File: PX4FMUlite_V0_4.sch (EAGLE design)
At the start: 126 parts, among them J2 DF13-4P-1.25V, J201 DF13C-6P-1.25V, J202 DF13C-6P-1.25V, J203 DF13C-6P-1.25V, J3 DF13C-4P-1.25V, J302 DF13C-4P-1.25V, J401 DF13C-4P-1.25V, J403 DF13C-7P-1.25V, J405 DF13C-4P-1.25V, J802 DF13C-3P-1.25V, M3_MOUNT1101 MOUNT-HOLE3.1MM, M3_MOUNT1102 MOUNT-HOLE3.1MM, M3_MOUNT1103 MOUNT-HOLE3.1MM, M3_MOUNT1104 MOUNT-HOLE3.1MM, U101 STM32F4X7VX, U2 MAX3051, U401 MAX3051, X101 3.2x2.5 mm / 24 MHz / 15 ppm

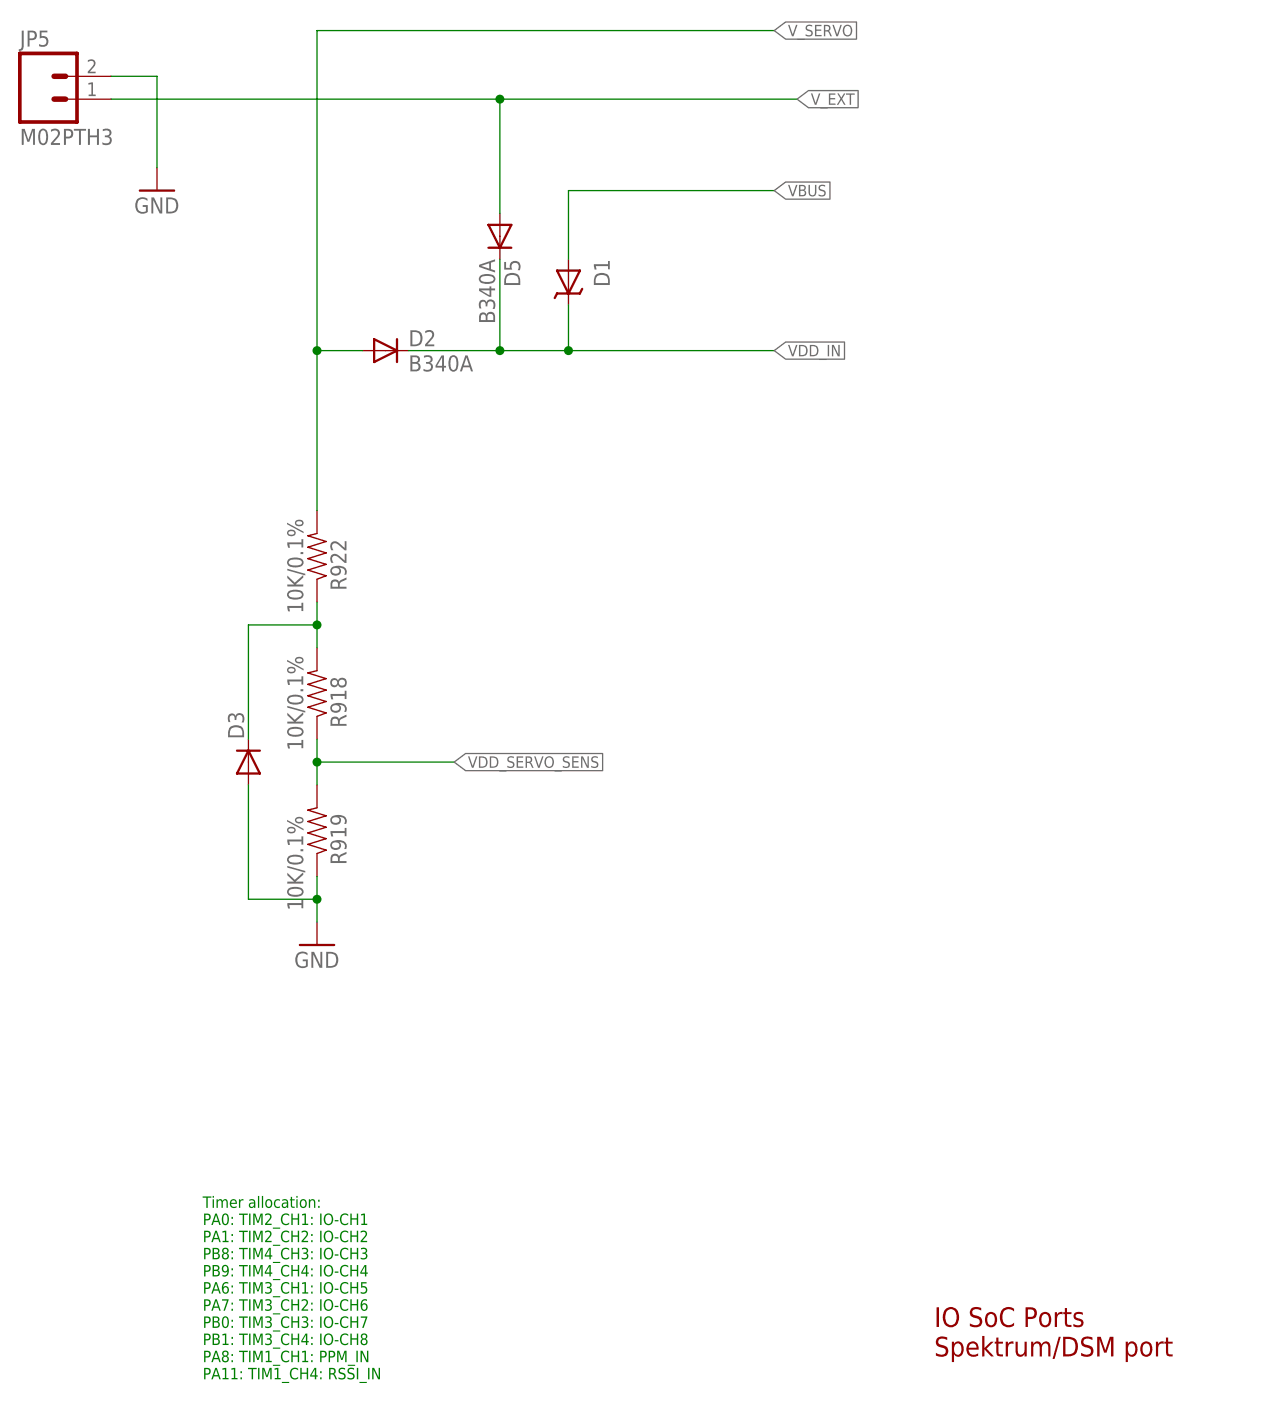
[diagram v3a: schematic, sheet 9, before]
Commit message: Voltage sense moved from VSERVO to VAUX
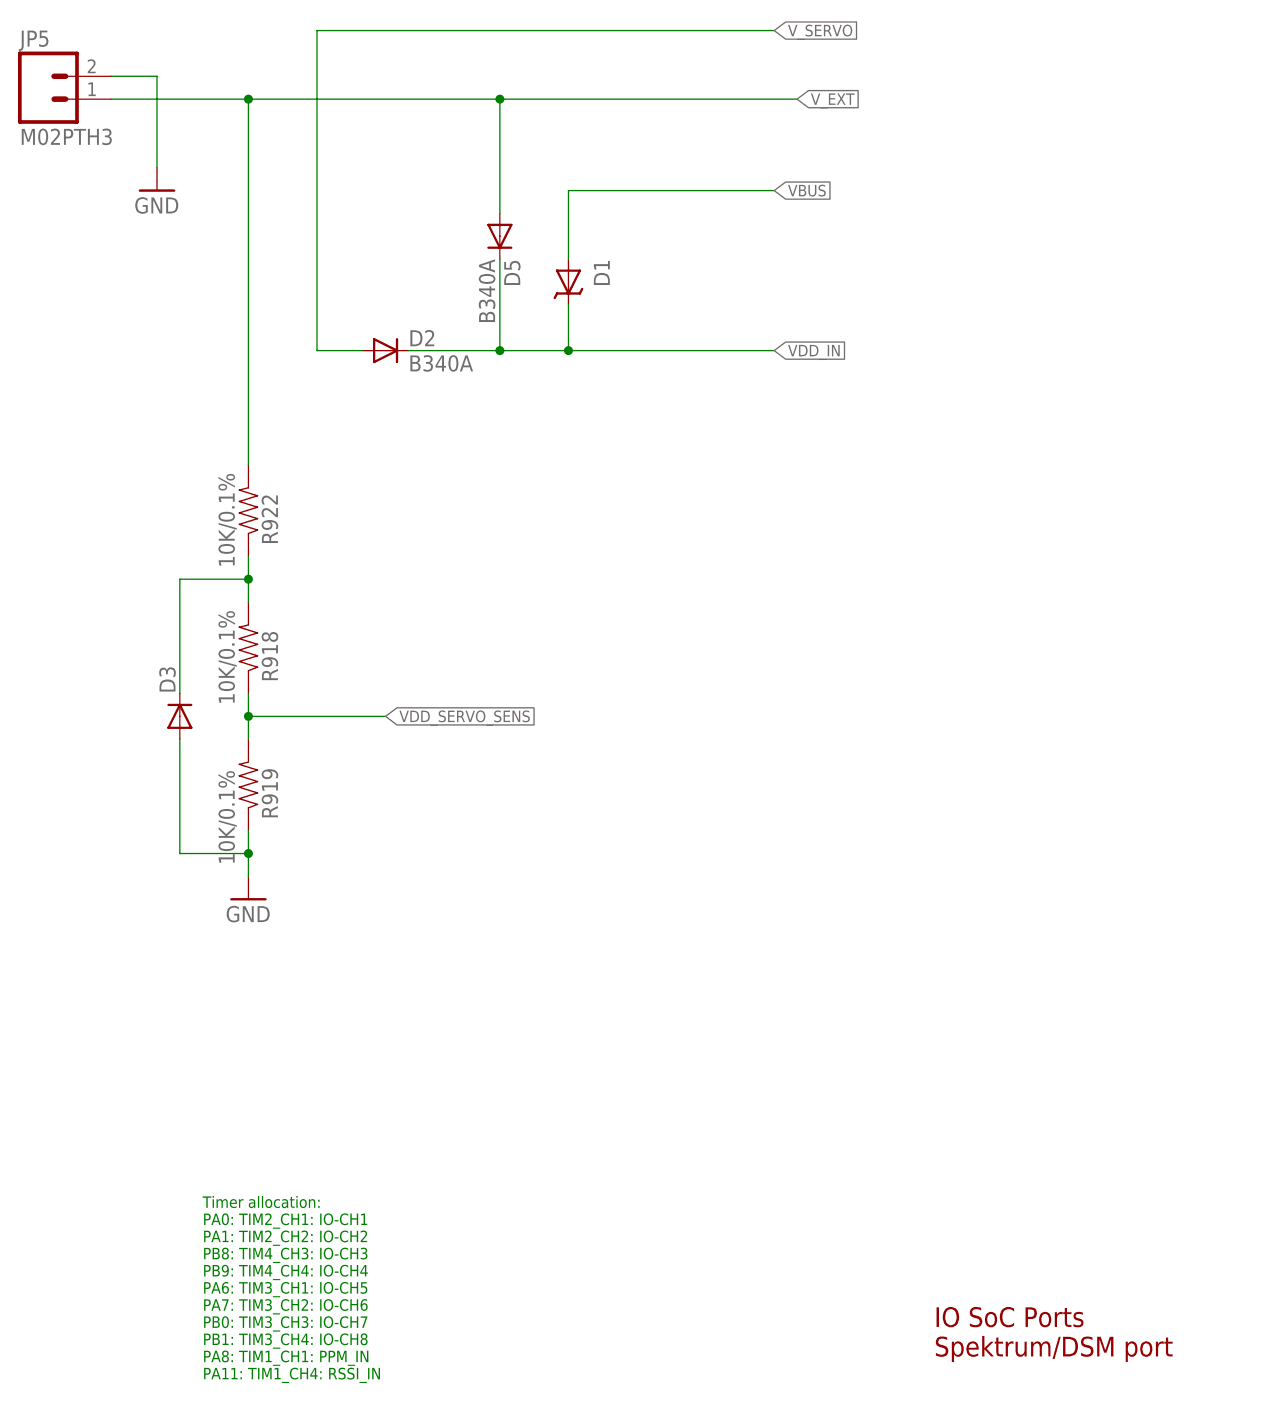
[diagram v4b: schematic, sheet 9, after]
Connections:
- net V_EXT: now also R922.2
- net V_SERVO: no longer R922.2
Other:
- moved on the sheet: D3, R918, R919, R922
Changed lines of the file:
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@@
 <instances>
 <instance part="FRAME4" gate="G$1" x="0" y="0"/>
-<instance part="R918" gate="G$1" x="96.52" y="88.9" smashed="yes" rot="MR90">
-<attribute name="PARTNO" x="96.52" y="88.9" size="1.778" layer="96" rot="MR90" display="off"/>
-<attribute name="NAME" x="98.0186" y="85.09" size="1.778" layer="95" rot="MR90"/>
-<attribute name="VALUE" x="93.218" y="82.55" size="1.778" layer="96" rot="MR90"/>
+<instance part="R918" gate="G$1" x="88.9" y="93.98" smashed="yes" rot="MR90">
+<attribute name="PARTNO" x="88.9" y="93.98" size="1.778" layer="96" rot="MR90" display="off"/>
+<attribute name="NAME" x="90.3986" y="90.17" size="1.778" layer="95" rot="MR90"/>
+<attribute name="VALUE" x="85.598" y="87.63" size="1.778" layer="96" rot="MR90"/>
 </instance>
-<instance part="R919" gate="G$1" x="96.52" y="73.66" smashed="yes" rot="MR90">
-<attribute name="PARTNO" x="96.52" y="73.66" size="1.778" layer="96" rot="MR90" display="off"/>
-<attribute name="NAME" x="98.0186" y="69.85" size="1.778" layer="95" rot="MR90"/>
-<attribute name="VALUE" x="93.218" y="64.77" size="1.778" layer="96" rot="MR90"/>
+<instance part="R919" gate="G$1" x="88.9" y="78.74" smashed="yes" rot="MR90">
+<attribute name="PARTNO" x="88.9" y="78.74" size="1.778" layer="96" rot="MR90" display="off"/>
+<attribute name="NAME" x="90.3986" y="74.93" size="1.778" layer="95" rot="MR90"/>
+<attribute name="VALUE" x="85.598" y="69.85" size="1.778" layer="96" rot="MR90"/>
 </instance>
-<instance part="GND52" gate="1" x="96.52" y="60.96"/>
-<instance part="R922" gate="G$1" x="96.52" y="104.14" smashed="yes" rot="MR90">
-<attribute name="PARTNO" x="96.52" y="104.14" size="1.778" layer="96" rot="MR90" display="off"/>
-<attribute name="NAME" x="98.0186" y="100.33" size="1.778" layer="95" rot="MR90"/>
-<attribute name="VALUE" x="93.218" y="97.79" size="1.778" layer="96" rot="MR90"/>
+<instance part="GND52" gate="1" x="88.9" y="66.04"/>
+<instance part="R922" gate="G$1" x="88.9" y="109.22" smashed="yes" rot="MR90">
+<attribute name="PARTNO" x="88.9" y="109.22" size="1.778" layer="96" rot="MR90" display="off"/>
+<attribute name="NAME" x="90.3986" y="105.41" size="1.778" layer="95" rot="MR90"/>
+<attribute name="VALUE" x="85.598" y="102.87" size="1.778" layer="96" rot="MR90"/>
 </instance>
 <instance part="D1" gate="G$1" x="124.46" y="134.62" smashed="yes" rot="MR270">
@@
 <attribute name="PARTNO" x="124.46" y="134.62" size="1.778" layer="96" rot="MR90" display="off"/>
 </instance>
-<instance part="D3" gate="G$1" x="88.9" y="81.28" rot="R90"/>
+<instance part="D3" gate="G$1" x="81.28" y="86.36" rot="R90"/>
 <instance part="D2" gate="G$1" x="104.14" y="127"/>
 <instance part="D5" gate="G$1" x="116.84" y="139.7" rot="R270"/>
@@
 <pinref part="GND52" gate="1" pin="GND"/>
 <pinref part="R919" gate="G$1" pin="1"/>
-<wire x1="96.52" y1="63.5" x2="96.52" y2="66.04" width="0.1524" layer="91"/>
+<wire x1="88.9" y1="68.58" x2="88.9" y2="71.12" width="0.1524" layer="91"/>
 <pinref part="D3" gate="G$1" pin="A"/>
-<wire x1="96.52" y1="66.04" x2="96.52" y2="68.58" width="0.1524" layer="91"/>
-<wire x1="96.52" y1="66.04" x2="88.9" y2="66.04" width="0.1524" layer="91"/>
-<wire x1="88.9" y1="66.04" x2="88.9" y2="78.74" width="0.1524" layer="91"/>
-<junction x="96.52" y="66.04"/>
+<wire x1="88.9" y1="71.12" x2="88.9" y2="73.66" width="0.1524" layer="91"/>
+<wire x1="88.9" y1="71.12" x2="81.28" y2="71.12" width="0.1524" layer="91"/>
+<wire x1="81.28" y1="71.12" x2="81.28" y2="83.82" width="0.1524" layer="91"/>
+<junction x="88.9" y="71.12"/>
 </segment>
 <segment>
@@
 <pinref part="R919" gate="G$1" pin="2"/>
 <pinref part="R918" gate="G$1" pin="1"/>
-<wire x1="96.52" y1="81.28" x2="96.52" y2="83.82" width="0.1524" layer="91"/>
-<wire x1="96.52" y1="78.74" x2="96.52" y2="81.28" width="0.1524" layer="91"/>
-<wire x1="96.52" y1="81.28" x2="111.76" y2="81.28" width="0.1524" layer="91"/>
-<label x="111.76" y="81.28" size="1.27" layer="95" rot="MR180" xref="yes"/>
-<junction x="96.52" y="81.28"/>
+<wire x1="88.9" y1="86.36" x2="88.9" y2="88.9" width="0.1524" layer="91"/>
+<wire x1="88.9" y1="83.82" x2="88.9" y2="86.36" width="0.1524" layer="91"/>
+<wire x1="88.9" y1="86.36" x2="104.14" y2="86.36" width="0.1524" layer="91"/>
+<label x="104.14" y="86.36" size="1.27" layer="95" rot="MR180" xref="yes"/>
+<junction x="88.9" y="86.36"/>
 </segment>
 </net>
@@
 <segment>
 <pinref part="D3" gate="G$1" pin="C"/>
-<wire x1="88.9" y1="83.82" x2="88.9" y2="96.52" width="0.1524" layer="91"/>
+<wire x1="81.28" y1="88.9" x2="81.28" y2="101.6" width="0.1524" layer="91"/>
 <pinref part="R918" gate="G$1" pin="2"/>
 <pinref part="R922" gate="G$1" pin="1"/>
-<wire x1="96.52" y1="93.98" x2="96.52" y2="96.52" width="0.1524" layer="91"/>
-<wire x1="96.52" y1="96.52" x2="96.52" y2="99.06" width="0.1524" layer="91"/>
-<wire x1="88.9" y1="96.52" x2="96.52" y2="96.52" width="0.1524" layer="91"/>
-<junction x="96.52" y="96.52"/>
+<wire x1="88.9" y1="99.06" x2="88.9" y2="101.6" width="0.1524" layer="91"/>
+<wire x1="88.9" y1="101.6" x2="88.9" y2="104.14" width="0.1524" layer="91"/>
+<wire x1="81.28" y1="101.6" x2="88.9" y2="101.6" width="0.1524" layer="91"/>
+<junction x="88.9" y="101.6"/>
 </segment>
 </net>
@@
 <wire x1="116.84" y1="154.94" x2="116.84" y2="142.24" width="0.1524" layer="91"/>
 <pinref part="JP5" gate="G$1" pin="1"/>
-<wire x1="73.66" y1="154.94" x2="116.84" y2="154.94" width="0.1524" layer="91"/>
+<wire x1="73.66" y1="154.94" x2="88.9" y2="154.94" width="0.1524" layer="91"/>
 <junction x="116.84" y="154.94"/>
+<pinref part="R922" gate="G$1" pin="2"/>
+<wire x1="88.9" y1="154.94" x2="116.84" y2="154.94" width="0.1524" layer="91"/>
+<wire x1="88.9" y1="114.3" x2="88.9" y2="154.94" width="0.1524" layer="91"/>
+<junction x="88.9" y="154.94"/>
 </segment>
 </net>
 <net name="V_SERVO" class="1">
 <segment>
-<pinref part="R922" gate="G$1" pin="2"/>
-<wire x1="96.52" y1="109.22" x2="96.52" y2="127" width="0.1524" layer="91"/>
 <wire x1="96.52" y1="127" x2="96.52" y2="162.56" width="0.1524" layer="91"/>
 <wire x1="96.52" y1="162.56" x2="147.32" y2="162.56" width="0.1524" layer="91"/>
-<junction x="96.52" y="127"/>
 <label x="147.32" y="162.56" size="1.27" layer="95" xref="yes"/>
 <pinref part="D2" gate="G$1" pin="A"/>
